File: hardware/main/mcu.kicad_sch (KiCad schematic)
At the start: 12 parts, among them Q9 SSM3J338R, U1 Holyiot-18010-NRF52840

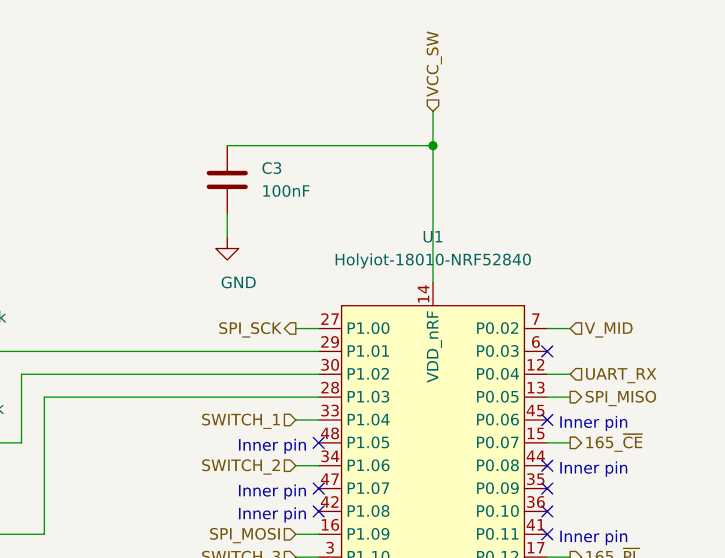
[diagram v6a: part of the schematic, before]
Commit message: Add V_BUS connection for the MCU board
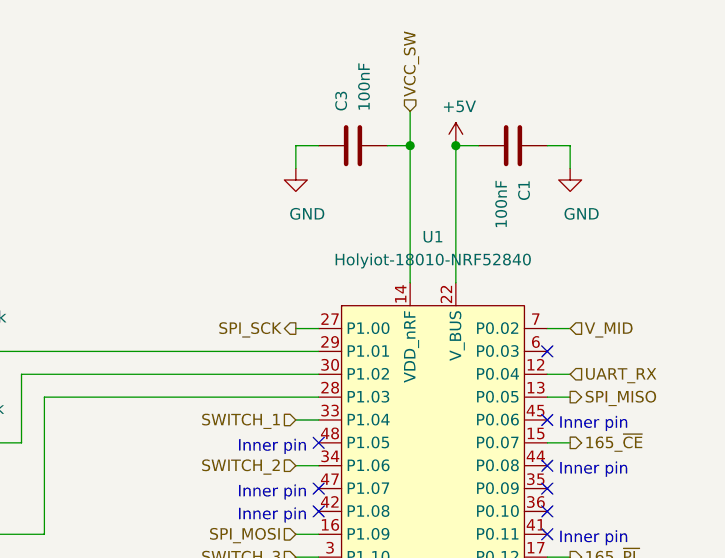
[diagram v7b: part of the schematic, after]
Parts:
- added C1: 100nF, Capacitor_SMD:C_0603_1608Metric_Pad1.08x0.95mm_HandSolder, symbol Device:C
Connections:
- net GND: now also C3.1, C1.1; no longer C3.2
- net VCC_SW: now also C3.2; no longer C3.1
- new net +5V: C1.2, U1.22 (V_BUS)
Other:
- moved on the sheet: C3
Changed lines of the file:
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@@
   (junction (at 52.07 138.43) (diameter 1.016) (color 0 0 0 0))
   (junction (at 52.07 168.91) (diameter 1.016) (color 0 0 0 0))
-  (junction (at 139.7 29.21) (diameter 1.016) (color 0 0 0 0))
+  (junction (at 137.16 29.21) (diameter 1.016) (color 0 0 0 0))
   (junction (at 139.7 130.81) (diameter 1.016) (color 0 0 0 0))
+  (junction (at 142.24 29.21) (diameter 1.016) (color 0 0 0 0))
   (no_connect (at 127 62.23))
   (no_connect (at 127 67.31))
@@
     (stroke (width 0) (type solid) (color 0 0 0 0))
   )
-  (wire (pts (xy 116.84 29.21) (xy 139.7 29.21))
-    (stroke (width 0) (type solid) (color 0 0 0 0))
-  )
-  (wire (pts (xy 116.84 36.83) (xy 116.84 39.37))
+  (wire (pts (xy 124.46 29.21) (xy 124.46 31.75))
     (stroke (width 0) (type solid) (color 0 0 0 0))
   )
@@
     (stroke (width 0) (type solid) (color 0 0 0 0))
   )
+  (wire (pts (xy 127 29.21) (xy 124.46 29.21))
+    (stroke (width 0) (type solid) (color 0 0 0 0))
+  )
   (wire (pts (xy 127 54.61) (xy 93.98 54.61))
     (stroke (width 0) (type solid) (color 0 0 0 0))
@@
     (stroke (width 0) (type solid) (color 0 0 0 0))
   )
+  (wire (pts (xy 134.62 29.21) (xy 137.16 29.21))
+    (stroke (width 0) (type solid) (color 0 0 0 0))
+  )
+  (wire (pts (xy 137.16 29.21) (xy 137.16 25.4))
+    (stroke (width 0) (type solid) (color 0 0 0 0))
+  )
+  (wire (pts (xy 137.16 44.45) (xy 137.16 29.21))
+    (stroke (width 0) (type solid) (color 0 0 0 0))
+  )
   (wire (pts (xy 137.16 128.27) (xy 137.16 130.81))
     (stroke (width 0) (type solid) (color 0 0 0 0))
@@
     (stroke (width 0) (type solid) (color 0 0 0 0))
   )
-  (wire (pts (xy 139.7 29.21) (xy 139.7 25.4))
-    (stroke (width 0) (type solid) (color 0 0 0 0))
-  )
-  (wire (pts (xy 139.7 44.45) (xy 139.7 29.21))
-    (stroke (width 0) (type solid) (color 0 0 0 0))
-  )
   (wire (pts (xy 139.7 128.27) (xy 139.7 130.81))
     (stroke (width 0) (type solid) (color 0 0 0 0))
@@
     (stroke (width 0) (type solid) (color 0 0 0 0))
   )
+  (wire (pts (xy 142.24 29.21) (xy 142.24 44.45))
+    (stroke (width 0) (type solid) (color 0 0 0 0))
+  )
+  (wire (pts (xy 142.24 29.21) (xy 144.78 29.21))
+    (stroke (width 0) (type solid) (color 0 0 0 0))
+  )
   (wire (pts (xy 142.24 130.81) (xy 142.24 128.27))
     (stroke (width 0) (type solid) (color 0 0 0 0))
   )
+  (wire (pts (xy 152.4 29.21) (xy 154.94 29.21))
+    (stroke (width 0) (type solid) (color 0 0 0 0))
+  )
   (wire (pts (xy 152.4 49.53) (xy 154.94 49.53))
     (stroke (width 0) (type solid) (color 0 0 0 0))
@@
   )
   (wire (pts (xy 152.4 123.19) (xy 170.18 123.19))
+    (stroke (width 0) (type solid) (color 0 0 0 0))
+  )
+  (wire (pts (xy 154.94 29.21) (xy 154.94 31.75))
     (stroke (width 0) (type solid) (color 0 0 0 0))
   )
@@
     (effects (font (size 1.27 1.27)) (justify right))
   )
-  (hierarchical_label "VCC_SW" (shape input) (at 139.7 25.4 90)
+  (hierarchical_label "VCC_SW" (shape input) (at 137.16 25.4 90)
     (effects (font (size 1.27 1.27)) (justify left))
   )
@@
     )
   )
+  (symbol (lib_id "power:+5V") (at 142.24 29.21 0) (unit 1)
+    (in_bom yes) (on_board yes)
+    (property "Reference" "#PWR0147" (id 0) (at 142.24 33.02 0)
+      (effects (font (size 1.27 1.27)) hide)
+    )
+    (property "Value" "+5V" (id 1) (at 142.6083 24.8856 0))
+    (property "Footprint" "" (id 2) (at 142.24 29.21 0)
+      (effects (font (size 1.27 1.27)) hide)
+    )
+    (property "Datasheet" "" (id 3) (at 142.24 29.21 0)
+      (effects (font (size 1.27 1.27)) hide)
+    )
+  )
   (symbol (lib_id "power:GND") (at 52.07 181.61 0) (unit 1)
     (in_bom yes) (on_board yes)
@@
     )
   )
-  (symbol (lib_id "power:GND") (at 116.84 39.37 0) (unit 1)
-    (in_bom yes) (on_board yes)
-    (property "Reference" "#PWR0109" (id 0) (at 116.84 45.72 0)
-      (effects (font (size 1.27 1.27)) hide)
-    )
-    (property "Value" "GND" (id 1) (at 118.11 44.45 0))
-    (property "Footprint" "" (id 2) (at 116.84 39.37 0)
-      (effects (font (size 1.27 1.27)) hide)
-    )
-    (property "Datasheet" "" (id 3) (at 116.84 39.37 0)
+  (symbol (lib_id "power:GND") (at 124.46 31.75 0) (unit 1)
+    (in_bom yes) (on_board yes)
+    (property "Reference" "#PWR0109" (id 0) (at 124.46 38.1 0)
+      (effects (font (size 1.27 1.27)) hide)
+    )
+    (property "Value" "GND" (id 1) (at 125.73 36.83 0))
+    (property "Footprint" "" (id 2) (at 124.46 31.75 0)
+      (effects (font (size 1.27 1.27)) hide)
+    )
+    (property "Datasheet" "" (id 3) (at 124.46 31.75 0)
       (effects (font (size 1.27 1.27)) hide)
     )
@@
     )
     (property "Datasheet" "" (id 3) (at 139.7 133.35 0)
+      (effects (font (size 1.27 1.27)) hide)
+    )
+  )
+  (symbol (lib_id "power:GND") (at 154.94 31.75 0) (unit 1)
+    (in_bom yes) (on_board yes)
+    (property "Reference" "#PWR0146" (id 0) (at 154.94 38.1 0)
+      (effects (font (size 1.27 1.27)) hide)
+    )
+    (property "Value" "GND" (id 1) (at 156.21 36.83 0))
+    (property "Footprint" "" (id 2) (at 154.94 31.75 0)
+      (effects (font (size 1.27 1.27)) hide)
+    )
+    (property "Datasheet" "" (id 3) (at 154.94 31.75 0)
       (effects (font (size 1.27 1.27)) hide)
     )
@@
     )
   )
-  (symbol (lib_id "Device:C") (at 116.84 33.02 0) (unit 1)
-    (in_bom yes) (on_board yes)
-    (property "Reference" "C3" (id 0) (at 120.65 31.75 0)
-      (effects (font (size 1.27 1.27)) (justify left))
-    )
-    (property "Value" "100nF" (id 1) (at 120.65 34.29 0)
-      (effects (font (size 1.27 1.27)) (justify left))
-    )
-    (property "Footprint" "Capacitor_SMD:C_0603_1608Metric_Pad1.08x0.95mm_HandSolder" (id 2) (at 117.8052 36.83 0)
-      (effects (font (size 1.27 1.27)) hide)
-    )
-    (property "Datasheet" "https://www.mouser.de/datasheet/2/40/X7RDielectric-777024.pdf" (id 3) (at 116.84 33.02 0)
-      (effects (font (size 1.27 1.27)) hide)
-    )
-    (property "Mouser" "581-06033C104KAT4A" (id 4) (at 116.84 33.02 0)
-      (effects (font (size 1.27 1.27)) hide)
-    )
-    (property "Part Name" "06033C104KAT4A " (id 5) (at 116.84 33.02 0)
-      (effects (font (size 1.27 1.27)) hide)
-    )
+  (symbol (lib_id "Device:C") (at 130.81 29.21 90) (unit 1)
+    (in_bom yes) (on_board yes)
+    (property "Reference" "C3" (id 0) (at 129.54 25.4 0)
+      (effects (font (size 1.27 1.27)) (justify left))
+    )
+    (property "Value" "100nF" (id 1) (at 132.08 25.4 0)
+      (effects (font (size 1.27 1.27)) (justify left))
+    )
+    (property "Footprint" "Capacitor_SMD:C_0603_1608Metric_Pad1.08x0.95mm_HandSolder" (id 2) (at 134.62 28.2448 0)
+      (effects (font (size 1.27 1.27)) hide)
+    )
+    (property "Datasheet" "https://www.mouser.de/datasheet/2/40/X7RDielectric-777024.pdf" (id 3) (at 130.81 29.21 0)
+      (effects (font (size 1.27 1.27)) hide)
+    )
+    (property "Mouser" "581-06033C104KAT4A" (id 4) (at 130.81 29.21 0)
+      (effects (font (size 1.27 1.27)) hide)
+    )
+    (property "Part Name" "06033C104KAT4A " (id 5) (at 130.81 29.21 0)
+      (effects (font (size 1.27 1.27)) hide)
+    )
+  )
+  (symbol (lib_id "Device:C") (at 148.59 29.21 270) (unit 1)
+    (in_bom yes) (on_board yes)
+    (property "Reference" "C1" (id 0) (at 149.86 33.02 0)
+      (effects (font (size 1.27 1.27)) (justify left))
+    )
+    (property "Value" "100nF" (id 1) (at 147.32 33.02 0)
+      (effects (font (size 1.27 1.27)) (justify left))
+    )
+    (property "Footprint" "Capacitor_SMD:C_0603_1608Metric_Pad1.08x0.95mm_HandSolder" (id 2) (at 144.78 30.1752 0)
+      (effects (font (size 1.27 1.27)) hide)
+    )
+    (property "Datasheet" "https://www.mouser.de/datasheet/2/40/X7RDielectric-777024.pdf" (id 3) (at 148.59 29.21 0)
+      (effects (font (size 1.27 1.27)) hide)
+    )
+    (property "Mouser" "581-06033C104KAT4A" (id 4) (at 148.59 29.21 0)
+      (effects (font (size 1.27 1.27)) hide)
+    )
+    (property "Part Name" "06033C104KAT4A " (id 5) (at 148.59 29.21 0)
+      (effects (font (size 1.27 1.27)) hide)
+    )

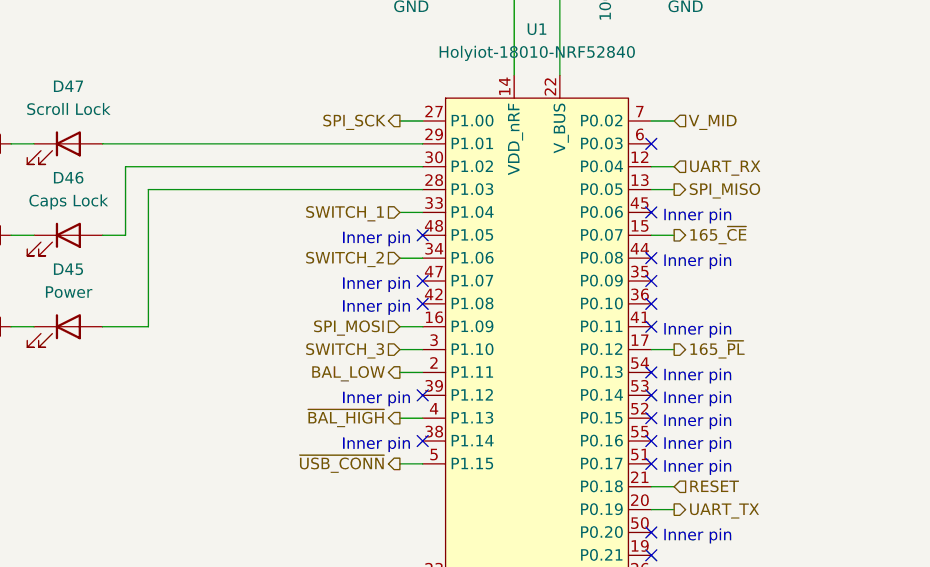
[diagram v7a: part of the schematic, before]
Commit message: Rework the off/bluetooth1/bluetooth2 switch connection
To save energy an external pull-down resistor is added and the off
position is not connected to the MCU.
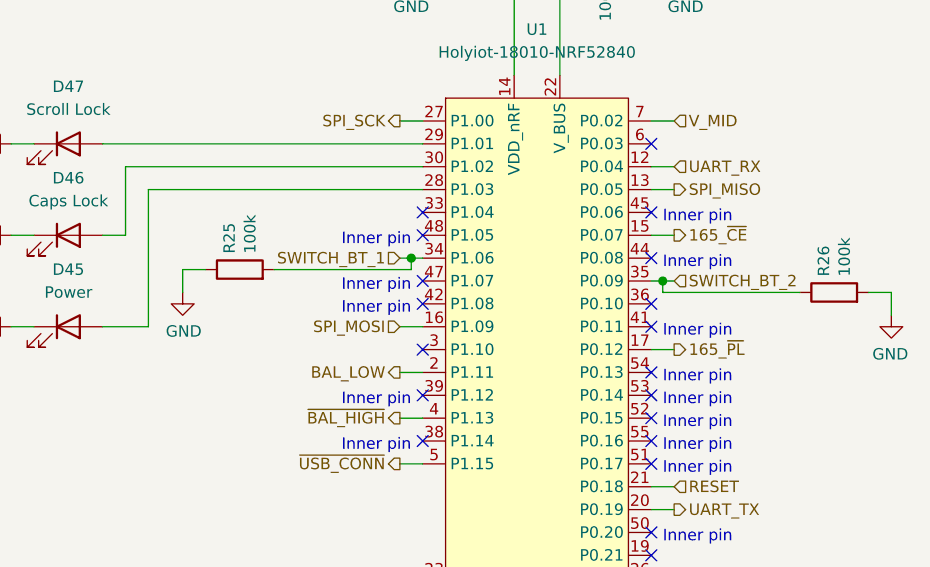
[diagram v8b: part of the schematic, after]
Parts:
- added R25, R26: 100k, Resistor_SMD:R_0603_1608Metric_Pad0.98x0.95mm_HandSolder, symbol Device:R
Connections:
- net GND: now also R25.1, R26.2
- net SWITCH_BT_2: now reaches U1.35 (P0.09)
- net SWITCH_BT_2: now also R26.1
- net SWITCH_1: no longer names the net of U1.33 (P1.04)
- net SWITCH_2 renamed SWITCH_BT_1
- net SWITCH_BT_1: now also R25.2
- net SWITCH_3: no longer names the net of U1.3 (P1.10)
- no-connect marks 25 -> 26
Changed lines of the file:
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@@
   (junction (at 52.07 138.43) (diameter 1.016) (color 0 0 0 0))
   (junction (at 52.07 168.91) (diameter 1.016) (color 0 0 0 0))
+  (junction (at 125.73 64.77) (diameter 1.016) (color 0 0 0 0))
   (junction (at 137.16 29.21) (diameter 1.016) (color 0 0 0 0))
   (junction (at 139.7 130.81) (diameter 1.016) (color 0 0 0 0))
   (junction (at 142.24 29.21) (diameter 1.016) (color 0 0 0 0))
+  (junction (at 153.67 67.31) (diameter 1.016) (color 0 0 0 0))
+  (no_connect (at 127 59.69))
   (no_connect (at 127 62.23))
   (no_connect (at 127 67.31))
   (no_connect (at 127 69.85))
+  (no_connect (at 127 74.93))
   (no_connect (at 127 80.01))
   (no_connect (at 127 85.09))
@@
   (no_connect (at 152.4 59.69))
   (no_connect (at 152.4 64.77))
-  (no_connect (at 152.4 67.31))
   (no_connect (at 152.4 69.85))
   (no_connect (at 152.4 72.39))
@@
     (stroke (width 0) (type solid) (color 0 0 0 0))
   )
+  (wire (pts (xy 100.33 66.04) (xy 100.33 68.58))
+    (stroke (width 0) (type solid) (color 0 0 0 0))
+  )
+  (wire (pts (xy 100.33 66.04) (xy 102.87 66.04))
+    (stroke (width 0) (type solid) (color 0 0 0 0))
+  )
+  (wire (pts (xy 110.49 66.04) (xy 125.73 66.04))
+    (stroke (width 0) (type solid) (color 0 0 0 0))
+  )
   (wire (pts (xy 124.46 29.21) (xy 124.46 31.75))
     (stroke (width 0) (type solid) (color 0 0 0 0))
@@
     (stroke (width 0) (type solid) (color 0 0 0 0))
   )
-  (wire (pts (xy 124.46 59.69) (xy 127 59.69))
-    (stroke (width 0) (type solid) (color 0 0 0 0))
-  )
-  (wire (pts (xy 124.46 64.77) (xy 127 64.77))
+  (wire (pts (xy 124.46 64.77) (xy 125.73 64.77))
     (stroke (width 0) (type solid) (color 0 0 0 0))
   )
@@
     (stroke (width 0) (type solid) (color 0 0 0 0))
   )
-  (wire (pts (xy 124.46 74.93) (xy 127 74.93))
-    (stroke (width 0) (type solid) (color 0 0 0 0))
-  )
   (wire (pts (xy 124.46 77.47) (xy 127 77.47))
     (stroke (width 0) (type solid) (color 0 0 0 0))
@@
     (stroke (width 0) (type solid) (color 0 0 0 0))
   )
+  (wire (pts (xy 125.73 64.77) (xy 125.73 66.04))
+    (stroke (width 0) (type solid) (color 0 0 0 0))
+  )
+  (wire (pts (xy 125.73 64.77) (xy 127 64.77))
+    (stroke (width 0) (type solid) (color 0 0 0 0))
+  )
   (wire (pts (xy 127 29.21) (xy 124.46 29.21))
     (stroke (width 0) (type solid) (color 0 0 0 0))
@@
     (stroke (width 0) (type solid) (color 0 0 0 0))
   )
+  (wire (pts (xy 152.4 67.31) (xy 153.67 67.31))
+    (stroke (width 0) (type solid) (color 0 0 0 0))
+  )
   (wire (pts (xy 152.4 74.93) (xy 154.94 74.93))
     (stroke (width 0) (type solid) (color 0 0 0 0))
@@
     (stroke (width 0) (type solid) (color 0 0 0 0))
   )
+  (wire (pts (xy 153.67 67.31) (xy 154.94 67.31))
+    (stroke (width 0) (type solid) (color 0 0 0 0))
+  )
+  (wire (pts (xy 153.67 68.58) (xy 153.67 67.31))
+    (stroke (width 0) (type solid) (color 0 0 0 0))
+  )
   (wire (pts (xy 154.94 29.21) (xy 154.94 31.75))
     (stroke (width 0) (type solid) (color 0 0 0 0))
   )
   (wire (pts (xy 154.94 57.15) (xy 152.4 57.15))
+    (stroke (width 0) (type solid) (color 0 0 0 0))
+  )
+  (wire (pts (xy 168.91 68.58) (xy 153.67 68.58))
+    (stroke (width 0) (type solid) (color 0 0 0 0))
+  )
+  (wire (pts (xy 179.07 68.58) (xy 176.53 68.58))
+    (stroke (width 0) (type solid) (color 0 0 0 0))
+  )
+  (wire (pts (xy 179.07 68.58) (xy 179.07 71.12))
     (stroke (width 0) (type solid) (color 0 0 0 0))
   )
@@
     (effects (font (size 1.27 1.27)) (justify right))
   )
-  (hierarchical_label "SWITCH_1" (shape input) (at 124.46 59.69 180)
-    (effects (font (size 1.27 1.27)) (justify right))
-  )
-  (hierarchical_label "SWITCH_2" (shape input) (at 124.46 64.77 180)
+  (hierarchical_label "SWITCH_BT_1" (shape input) (at 124.46 64.77 180)
     (effects (font (size 1.27 1.27)) (justify right))
   )
@@
     (effects (font (size 1.27 1.27)) (justify right))
   )
-  (hierarchical_label "SWITCH_3" (shape input) (at 124.46 74.93 180)
-    (effects (font (size 1.27 1.27)) (justify right))
-  )
   (hierarchical_label "BAL_LOW" (shape output) (at 124.46 77.47 180)
     (effects (font (size 1.27 1.27)) (justify right))
@@
   )
   (hierarchical_label "165_~CE" (shape output) (at 154.94 62.23 0)
+    (effects (font (size 1.27 1.27)) (justify left))
+  )
+  (hierarchical_label "SWITCH_BT_2" (shape input) (at 154.94 67.31 0)
     (effects (font (size 1.27 1.27)) (justify left))
   )
@@
     )
   )
+  (symbol (lib_id "power:GND") (at 100.33 68.58 0) (unit 1)
+    (in_bom yes) (on_board yes)
+    (property "Reference" "#PWR0148" (id 0) (at 100.33 74.93 0)
+      (effects (font (size 1.27 1.27)) hide)
+    )
+    (property "Value" "GND" (id 1) (at 100.4443 72.9044 0))
+    (property "Footprint" "" (id 2) (at 100.33 68.58 0)
+      (effects (font (size 1.27 1.27)) hide)
+    )
+    (property "Datasheet" "" (id 3) (at 100.33 68.58 0)
+      (effects (font (size 1.27 1.27)) hide)
+    )
+  )
   (symbol (lib_id "power:GND") (at 124.46 31.75 0) (unit 1)
     (in_bom yes) (on_board yes)
@@
     )
     (property "Datasheet" "" (id 3) (at 154.94 31.75 0)
+      (effects (font (size 1.27 1.27)) hide)
+    )
+  )
+  (symbol (lib_id "power:GND") (at 179.07 71.12 0) (mirror y) (unit 1)
+    (in_bom yes) (on_board yes)
+    (property "Reference" "#PWR?" (id 0) (at 179.07 77.47 0)
+      (effects (font (size 1.27 1.27)) hide)
+    )
+    (property "Value" "GND" (id 1) (at 178.9557 75.4444 0))
+    (property "Footprint" "" (id 2) (at 179.07 71.12 0)
+      (effects (font (size 1.27 1.27)) hide)
+    )
+    (property "Datasheet" "" (id 3) (at 179.07 71.12 0)
       (effects (font (size 1.27 1.27)) hide)
     )
@@
       (effects (font (size 1.27 1.27)) hide)
     )
+  )
+  (symbol (lib_id "Device:R") (at 106.68 66.04 90) (unit 1)
+    (in_bom yes) (on_board yes)
+    (property "Reference" "R25" (id 0) (at 105.5306 64.2619 0)
+      (effects (font (size 1.27 1.27)) (justify left))
+    )
+    (property "Value" "100k" (id 1) (at 107.8293 64.2619 0)
+      (effects (font (size 1.27 1.27)) (justify left))
+    )
+    (property "Footprint" "Resistor_SMD:R_0603_1608Metric_Pad0.98x0.95mm_HandSolder" (id 2) (at 106.68 67.818 90)
+      (effects (font (size 1.27 1.27)) hide)
+    )
+    (property "Datasheet" "~" (id 3) (at 106.68 66.04 0)
+      (effects (font (size 1.27 1.27)) hide)
+    )
+  )
+  (symbol (lib_id "Device:R") (at 172.72 68.58 90) (unit 1)
+    (in_bom yes) (on_board yes)
+    (property "Reference" "R26" (id 0) (at 171.5706 66.8019 0)
+      (effects (font (size 1.27 1.27)) (justify left))
+    )
+    (property "Value" "100k" (id 1) (at 173.8693 66.8019 0)
+      (effects (font (size 1.27 1.27)) (justify left))
+    )
+    (property "Footprint" "Resistor_SMD:R_0603_1608Metric_Pad0.98x0.95mm_HandSolder" (id 2) (at 172.72 70.358 90)
+      (effects (font (size 1.27 1.27)) hide)
+    )
+    (property "Datasheet" "~" (id 3) (at 172.72 68.58 0)
+      (effects (font (size 1.27 1.27)) hide)
+    )
